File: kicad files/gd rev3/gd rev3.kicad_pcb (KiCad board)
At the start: 4 copper layers, 165.9 x 190.6 mm, 286 parts, among them J1 XY, J10 Apple_II_Slot, J11 Game Port, J12 Right Angle, J13 SWD, J14 USB_A, J15 Rev2 Header, J16 RP2040 Header, J17 VGA_Micro, J18 vga_SWD, J19 SPKR, J2 DB19_4, J20 Ears, J21 KBD Serial, J22 L77HDE15SD1CH4F, J23 Game-DB VERIFY FOOTPRINT, J3 DB19_16, J4 EN, J5 DSUB19, J6 FDC Hdr, J7 EN, J8 EN, J9 IO-Xtra, Q1 BC817, Q2 BC817, Q3 BC817, Q4 BC817, Q5 BC817, Q6 BC817, Q7 BC817, Q8 BC817, Q9 BC817, SW1 MEGA RESET, SW2 DEV, SW3 IOSEL, SW4 KBD RESET, SW5 KBD Boot Sel, SW6 VGA Boot Sel, SW7 VGA RESET, U1 Apple_MEGA_II, U10 DRAM64KX4, U11 IWM, U12 Slotmaker, U13 74HCT245, U14 RP2040, U15 MIC5504-3.3YM5, U16 74HC245, U17 W25Q128JVS, U18 HCT251, U19 W25Q128JVS, U2 w65c02s, U20 NE556, U21 NE556, U22 74HCT245, U23 RP2040, U24 74LVC2G04, U26 MCP4541T, U27 LM4875, U28 SN74LVC573ANS, U29 74LVC2G04, U3 74LVC1G02, U30 74LVC2G04, U32 LM7905_TO220, U35 74LVC2G04, U4 74HCT245, U5 74HCT245, U6 AT28C256-PLCC, U7 DRAM64KX4, U8 DRAM64KX4, U9 DRAM64KX4, X1 14.31818MHz, Y1 ECS-120-18-33-JEM-TR, Y2 ECS-120-18-33-JEM-TR

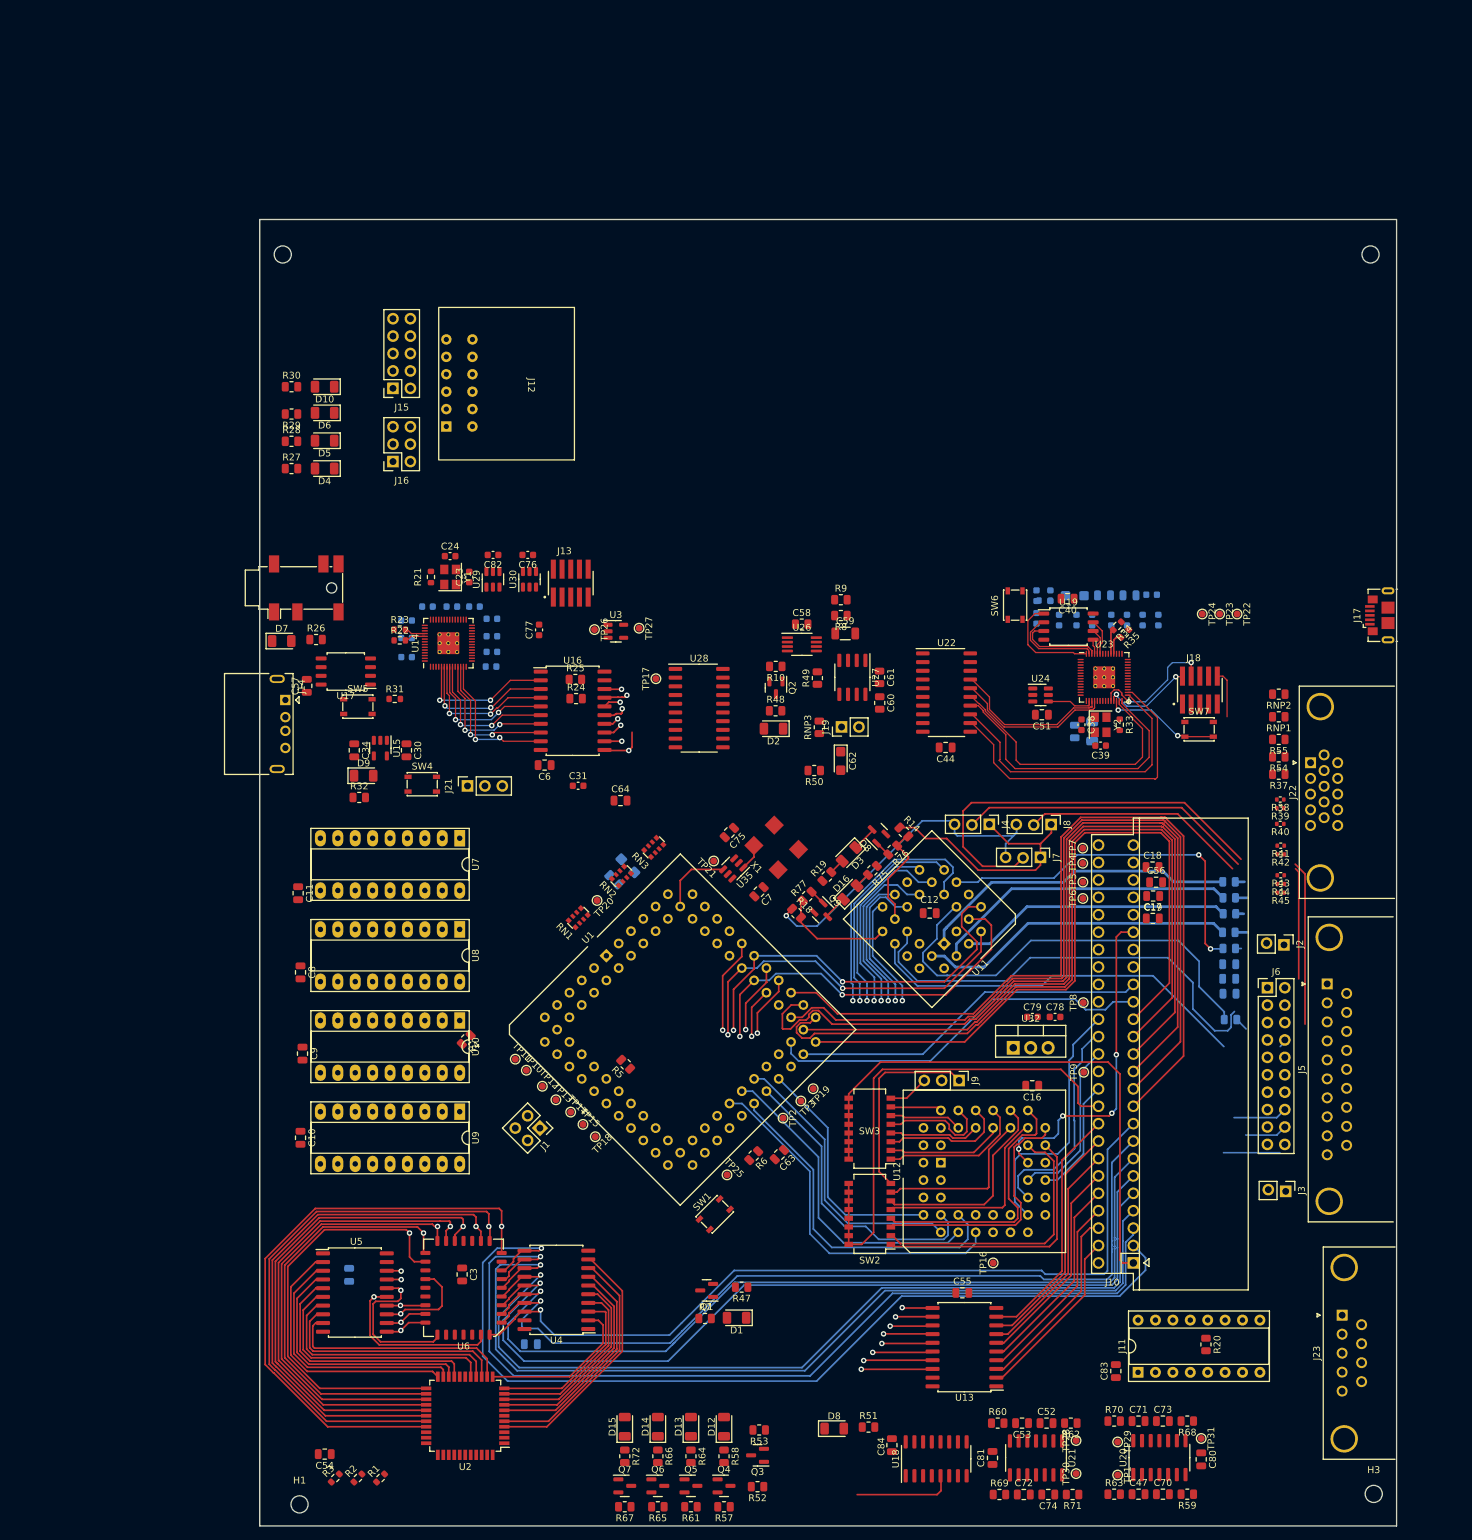
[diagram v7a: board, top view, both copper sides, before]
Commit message: moved some pasives to back side, looking for more board dimension optimizations
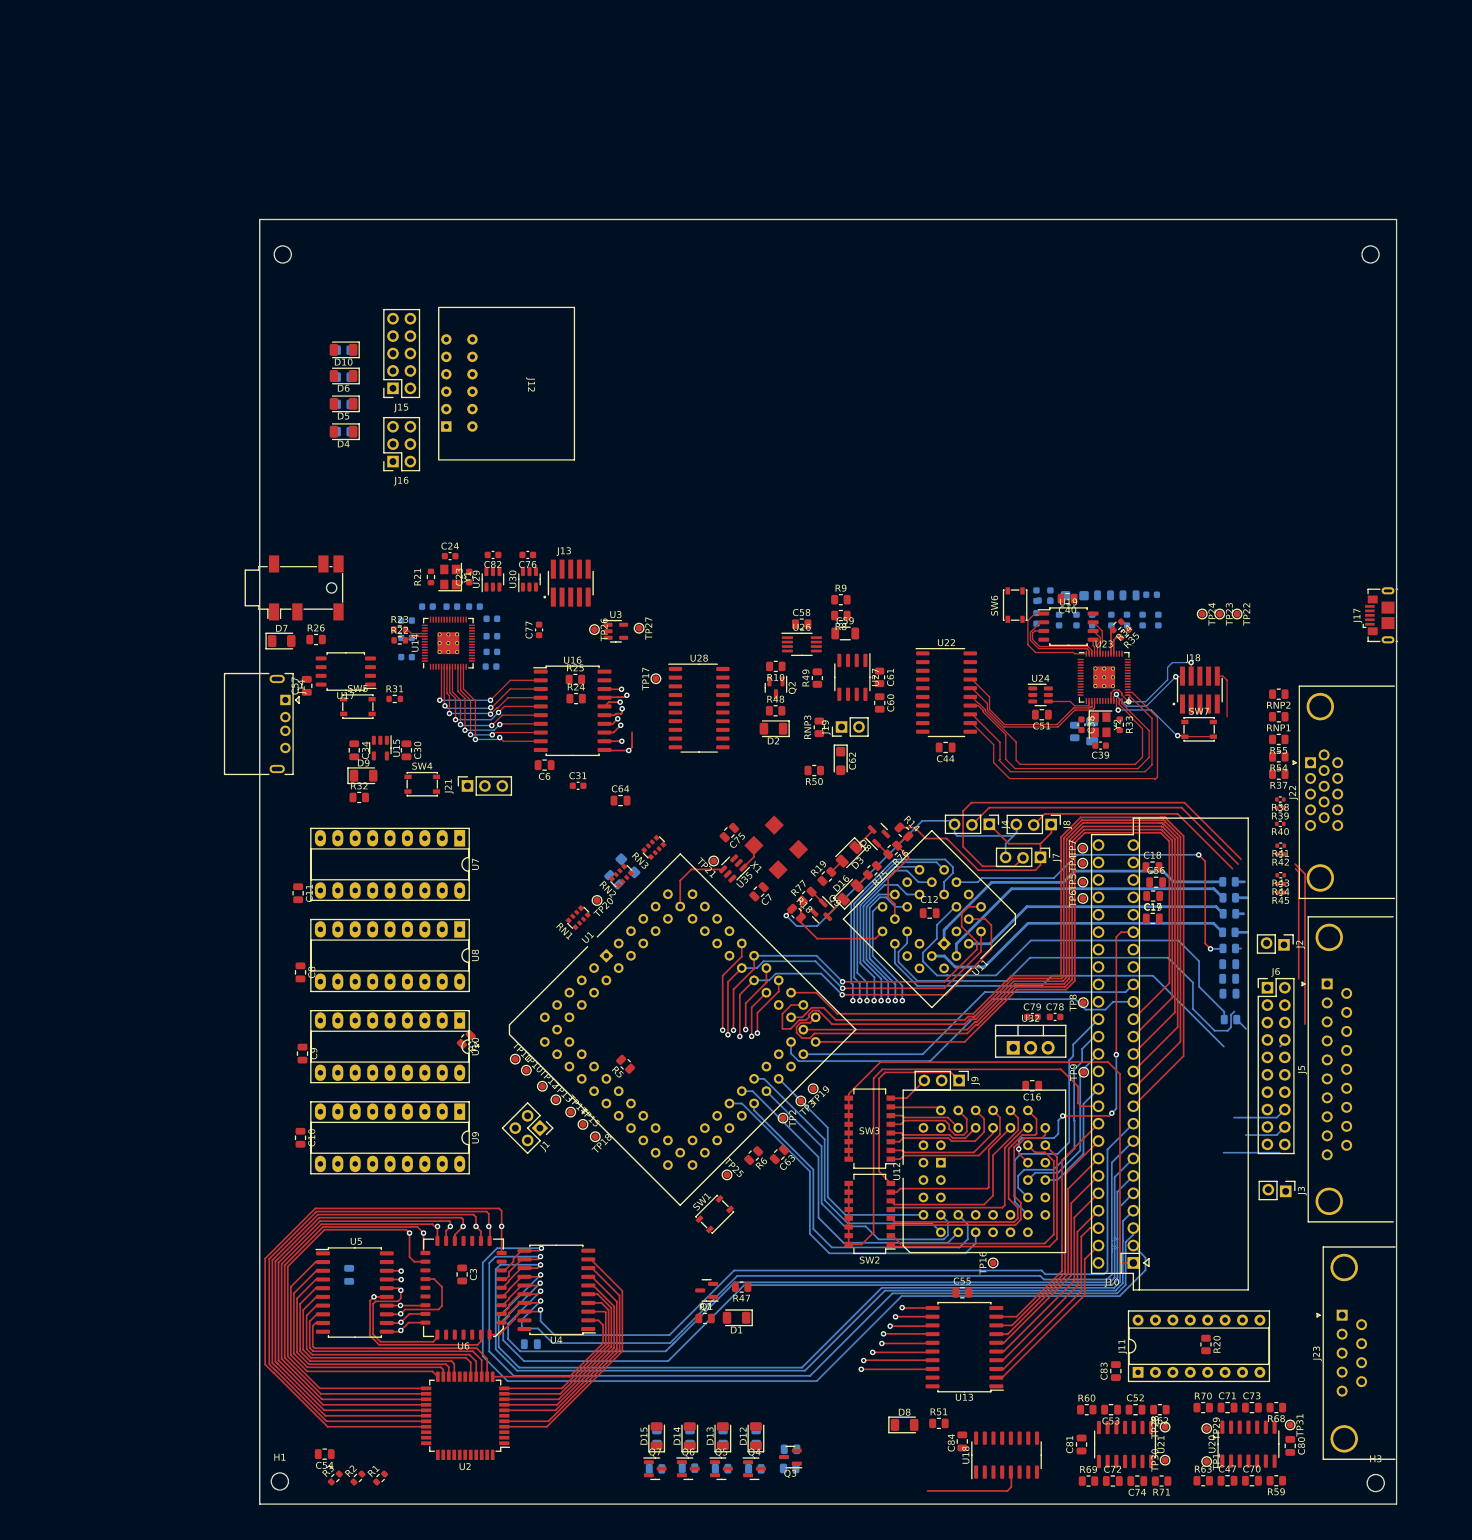
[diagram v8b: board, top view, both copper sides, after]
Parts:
- R27, R28, R29, R30, R52, R53, R57, R58, R61, R64, R65, R66, R67, R72: moved to B.Cu
- moved C52 13.1 mm to (188.6, 229.5)
- moved C53 13.1 mm to (185.0, 229.5)
- moved R60 13.1 mm to (181.4, 229.5)
- moved R62 13.1 mm to (192.1, 229.5)
- moved TP31 13.1 mm to (211.1, 231.7)
- moved C47 13.1 mm to (202.0, 239.9)
- moved C70 13.1 mm to (205.5, 239.9)
- moved C71 13.1 mm to (202.0, 229.2)
- moved C72 13.1 mm to (185.3, 239.9)
- moved C73 13.1 mm to (205.5, 229.2)
- moved C74 13.1 mm to (188.8, 239.9)
- moved C80 13.1 mm to (211.1, 234.8)
- moved C81 13.1 mm to (180.7, 234.6)
- moved R59 13.1 mm to (209.1, 239.9)
- moved R63 13.1 mm to (198.4, 239.9)
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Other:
- board size 165.9 x 190.6 mm -> 165.9 x 187.4 mm
